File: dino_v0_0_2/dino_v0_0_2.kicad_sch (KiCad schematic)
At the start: 27 parts, among them Q1 Write Button Gate, U1 Quad AND

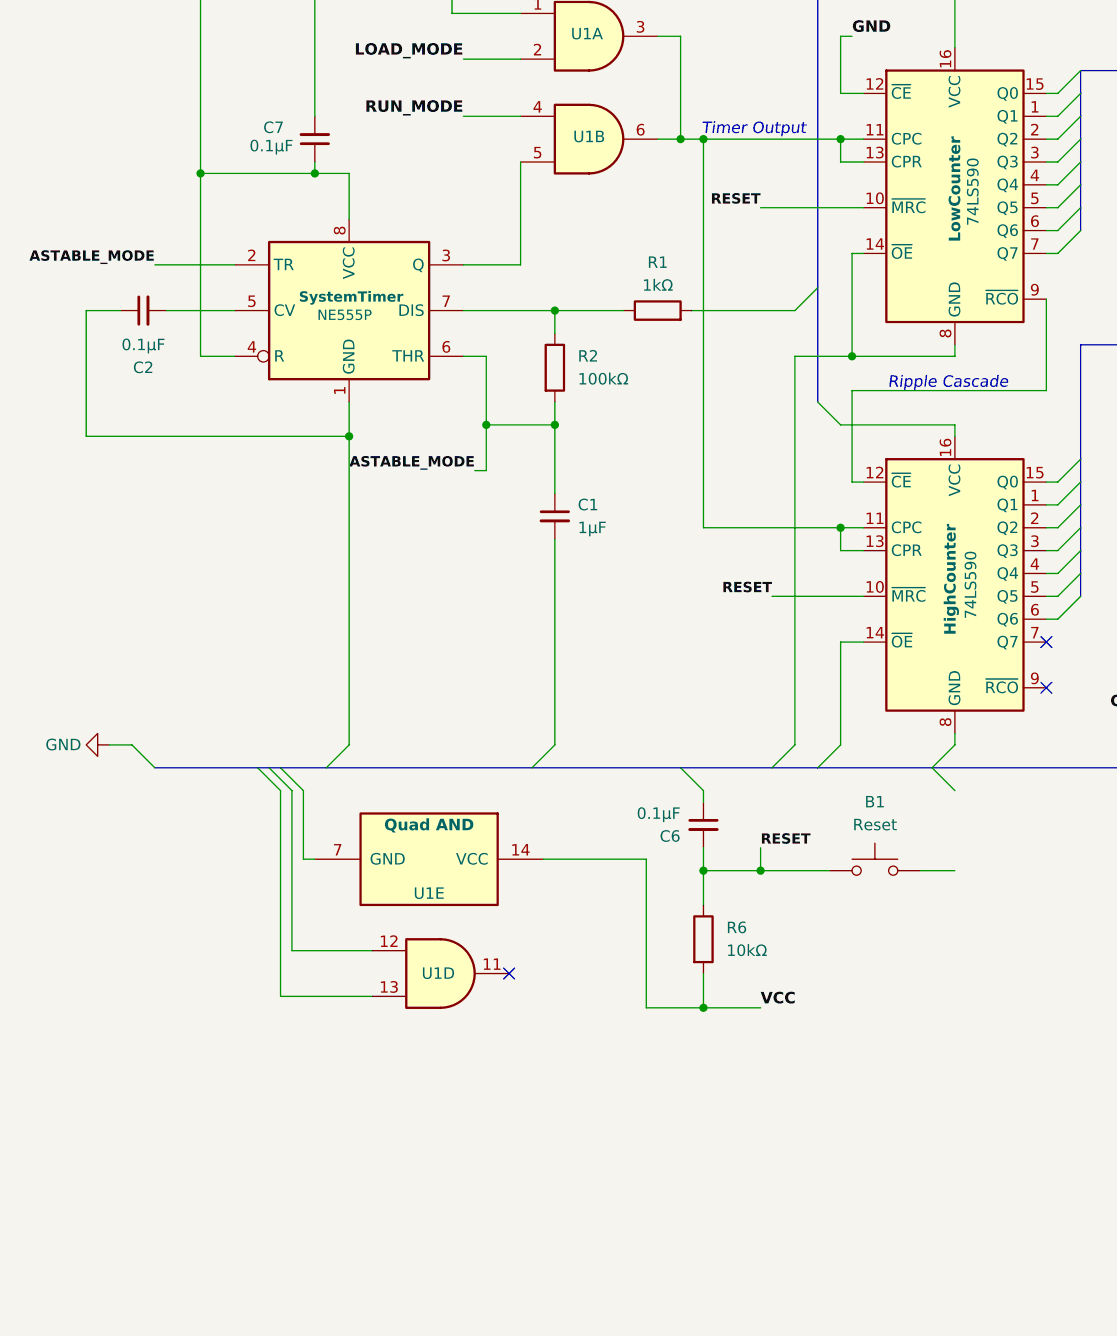
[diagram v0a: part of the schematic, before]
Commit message: Migrates project to version 0.0.2 with Ring Counter addition
Renames existing project files from version 0.0.1 to 0.0.2 to reflect updates.
Adds a new sub-circuit named "RingCounter" to the schematic, improving functionality.
Updates date and revision information in title blocks to keep documentation current.
Integrates new wires, junctions, and labels into existing schematics to accommodate the RingCounter.
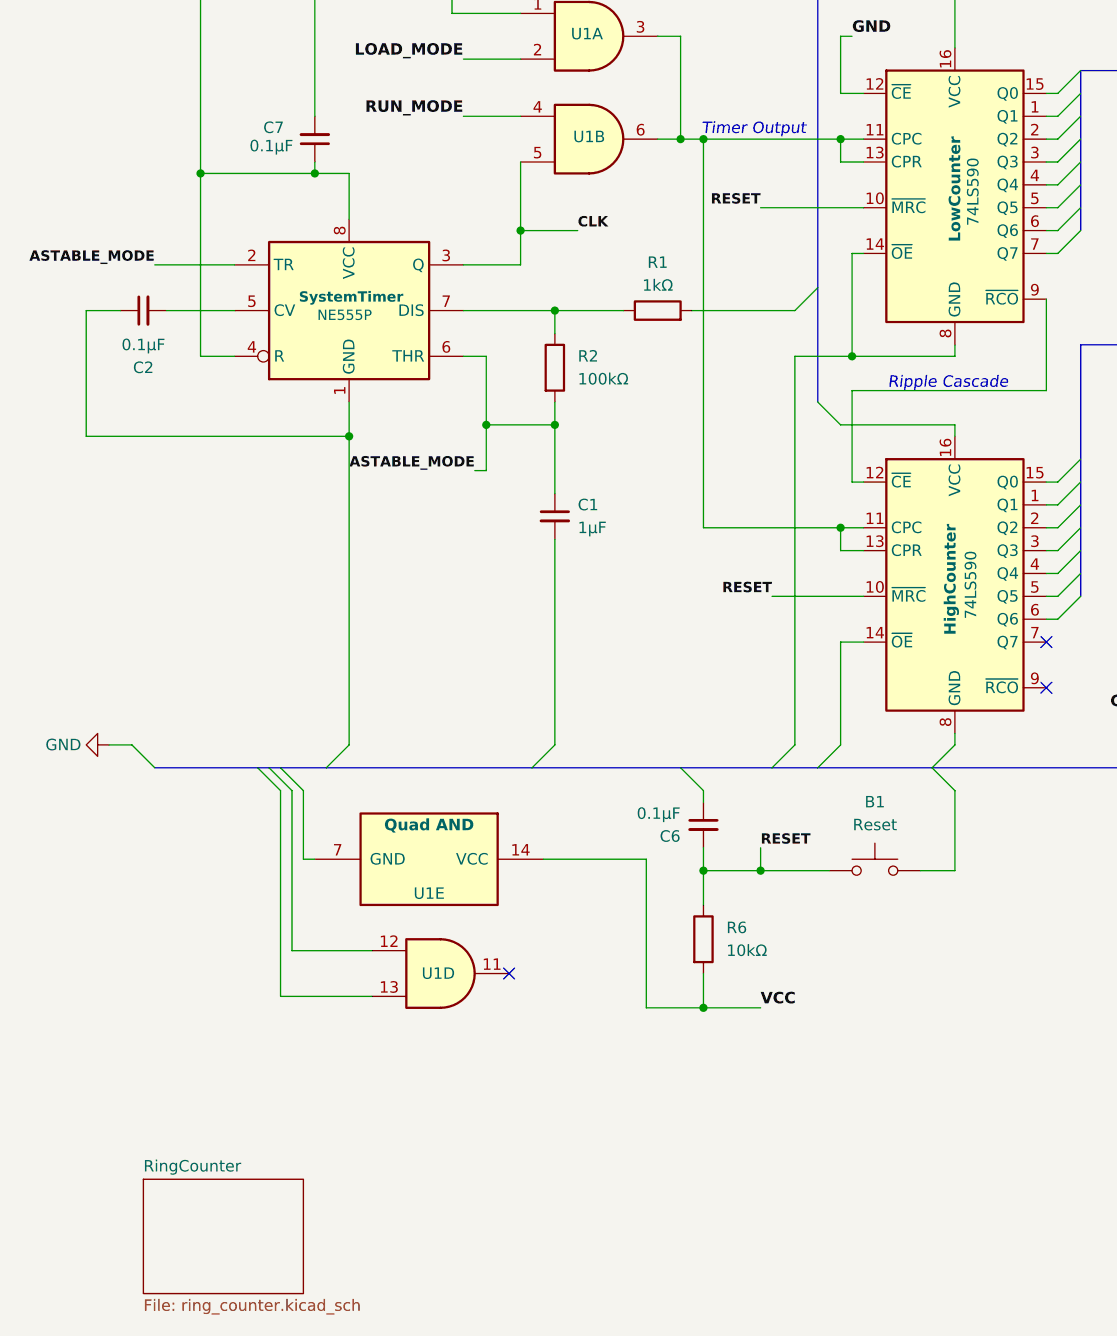
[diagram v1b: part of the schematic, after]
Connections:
- net CLK: now reaches SystemTimer.3 (Q), U1.5
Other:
- added sheet RingCounter (ring_counter.kicad_sch)
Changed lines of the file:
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@@
 	(title_block
 		(title "Dino v0.0.1")
-		(date "2025-07-02")
-		(rev "v1.0.3")
+		(date "2025-07-18")
+		(rev "v1.0.4")
 		(comment 1 "Core Components")
 		(comment 3 "Utilizes a 555 timer and binary counter to increment addressing.")
@@
 	)
 	(junction
+		(at 67.31 72.39)
+		(diameter 0)
+		(color 0 0 0 0)
+	)
+	(junction
 		(at 199.39 69.85)
 		(diameter 0)
@@
 	(wire
 		(pts
+			(xy 67.31 72.39) (xy 73.66 72.39)
+		)
+		(stroke
+			(width 0)
+			(type default)
+		)
+	)
+	(wire
+		(pts
 			(xy 97.79 86.36) (xy 104.14 86.36)
 		)
@@
 	(wire
 		(pts
-			(xy 67.31 76.2) (xy 67.31 64.77)
+			(xy 67.31 76.2) (xy 67.31 72.39)
 		)
 		(stroke
@@
 	(wire
 		(pts
+			(xy 67.31 72.39) (xy 67.31 64.77)
+		)
+		(stroke
+			(width 0)
+			(type default)
+		)
+	)
+	(wire
+		(pts
 			(xy 19.05 95.25) (xy 48.26 95.25)
 		)
@@
 	(wire
 		(pts
+			(xy 115.57 134.62) (xy 115.57 143.51)
+		)
+		(stroke
+			(width 0)
+			(type default)
+		)
+	)
+	(wire
+		(pts
 			(xy 125.73 100.33) (xy 127 100.33)
 		)
@@
 		)
 	)
+	(label "CLK"
+		(at 73.66 72.39 0)
+		(effects
+			(font
+				(size 1.143 1.143)
+				(thickness 0.254)
+				(bold yes)
+			)
+			(justify left bottom)
+		)
+	)
 	(label "LOAD_MODE"
 		(at 60.96 53.34 180)
@@
 				)
 			)
+		)
+	)
+	(sheet
+		(at 25.4 177.8)
+		(size 17.78 12.7)
+		(exclude_from_sim no)
+		(in_bom yes)
+		(on_board yes)
+		(dnp no)
+		(fields_autoplaced yes)
+		(stroke
+			(width 0.1524)
+			(type solid)
+		)
+		(fill
+			(color 0 0 0 0.0000)
+		)
+		(property "Sheetname" "RingCounter"
+			(at 25.4 177.0884 0)
+			(effects
+				(font
+					(size 1.27 1.27)
+				)
+				(justify left bottom)
+			)
+		)
+		(property "Sheetfile" "ring_counter.kicad_sch"
+			(at 25.4 191.0846 0)
+			(effects
+				(font
+					(size 1.27 1.27)
+				)
+				(justify left top)
+			)
+		)
+		(instances
+			(project "dino_v0_0_1"
+				(path "/e43166a5-d972-471d-b3cf-9f4f12c7f541"
+					(page "3")
+				)
+			)

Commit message: Dino v0.0.2 Schematic Update
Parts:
- removed B1: Reset, symbol Switch:SW_Push
- removed B2: Write, symbol Switch:SW_Push
- removed B3: Inc Addr, symbol Switch:SW_Push
- removed Bus-Arbiter: 74LS645, symbol 74xx:74LS645
- removed C3, C4, C5, C6: 0.1µF, symbol Device:C_Small
- removed HighCounter, LowCounter: 74LS590, symbol 74xx:74LS590
- removed MCM60256AP: SRAM, symbol Memory_RAM:MCM60256AP
- removed Q1: Write Button Gate, Package_TO_SOT_THT:TO-92_Inline, symbol Transistor_BJT:2N3904
- removed R3, R4, R5, R6, R7, R8: 10kΩ, symbol Device:R
- removed SPDT: LOAD/RUN, symbol Switch:SW_SPDT
- removed U1: Quad AND, symbol 74xx:74LS08
- added U5: 7400, symbol 74xx:7400
- added U6: 74LS163, symbol 74xx:74LS163
- added U7: 74LS138, symbol 74xx:74LS138
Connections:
- net GND: now also C1.2, C2.1, C7.1, SystemTimer.1 (GND), U5.7 (GND), U6.3 (D0), U6.4 (D1), U6.5 (D2), U6.6 (D3), U6.8 (GND), U7.4 (E1), U7.5 (E2), U7.8 (GND); no longer C7.2
- net +5V: now reaches SystemTimer.4 (R), SystemTimer.8 (VCC)
- net +5V: now also C7.2, C8.2, R1.2, U5.14 (VCC), U6.10 (CET), U6.16 (VCC), U6.7 (CEP), U6.9 (~{PE}), U7.16 (VCC), U7.6 (E3); no longer C7.1
- net ASTABLE_MODE: no longer names the net of C1.1, R2.2, SystemTimer.2 (TR), SystemTimer.6 (THR)
- net CLK: no longer names the net of SystemTimer.3 (Q)
- net CLK: now also U6.2 (CP)
- new net: U6.14 (Q0), U7.1 (A0)
- new net: U5.1, U6.13 (Q1), U7.2 (A1)
- new net: U5.2, U6.12 (Q2), U7.3 (A2)
- new net: U5.3, U6.1 (~{MR})
- no-connect marks 3 -> 19
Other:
- sheet RingCounter renamed Data
- sheet Data: file ring_counter.kicad_sch -> data.kicad_sch
- note removed: "+5V"
- note removed: "Output Enable"
- note removed: "Ripple Cascade"
- note removed: "Timer Output"
- note removed: "Write Pulse"
- title: Dino v0.0.1 -> Dino v0.0.2
- moved on the sheet: C1, C2, C7, R1, R2, SystemTimer

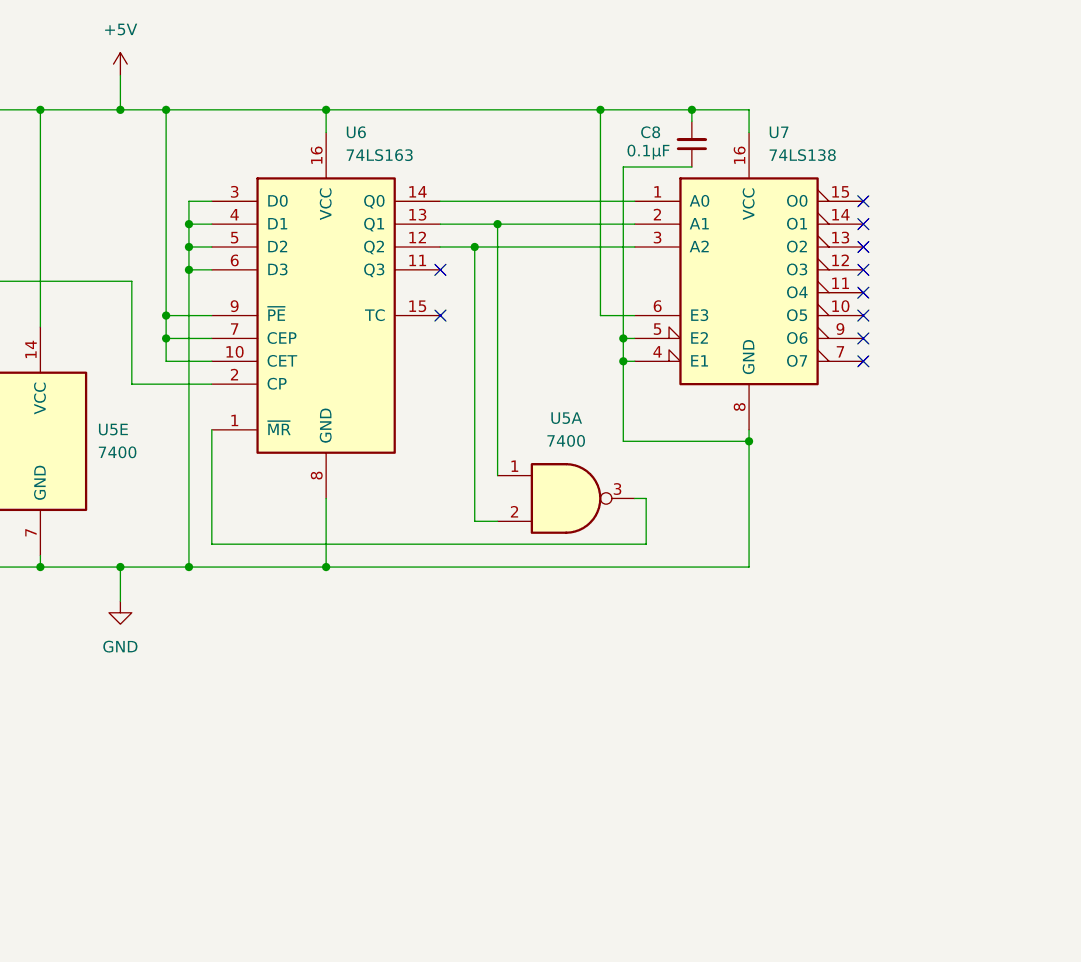
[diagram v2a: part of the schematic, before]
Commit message: Updates schematics for improved circuit design
Revises date and revision comments across schematics for consistency
Modifies component descriptions to reflect accurate functionality
Adds new junctions and wires for improved connectivity in the circuit
Inserts new capacitors and logic decoders to enhance circuit performance

Includes changes to the title block and project metadata for clarity
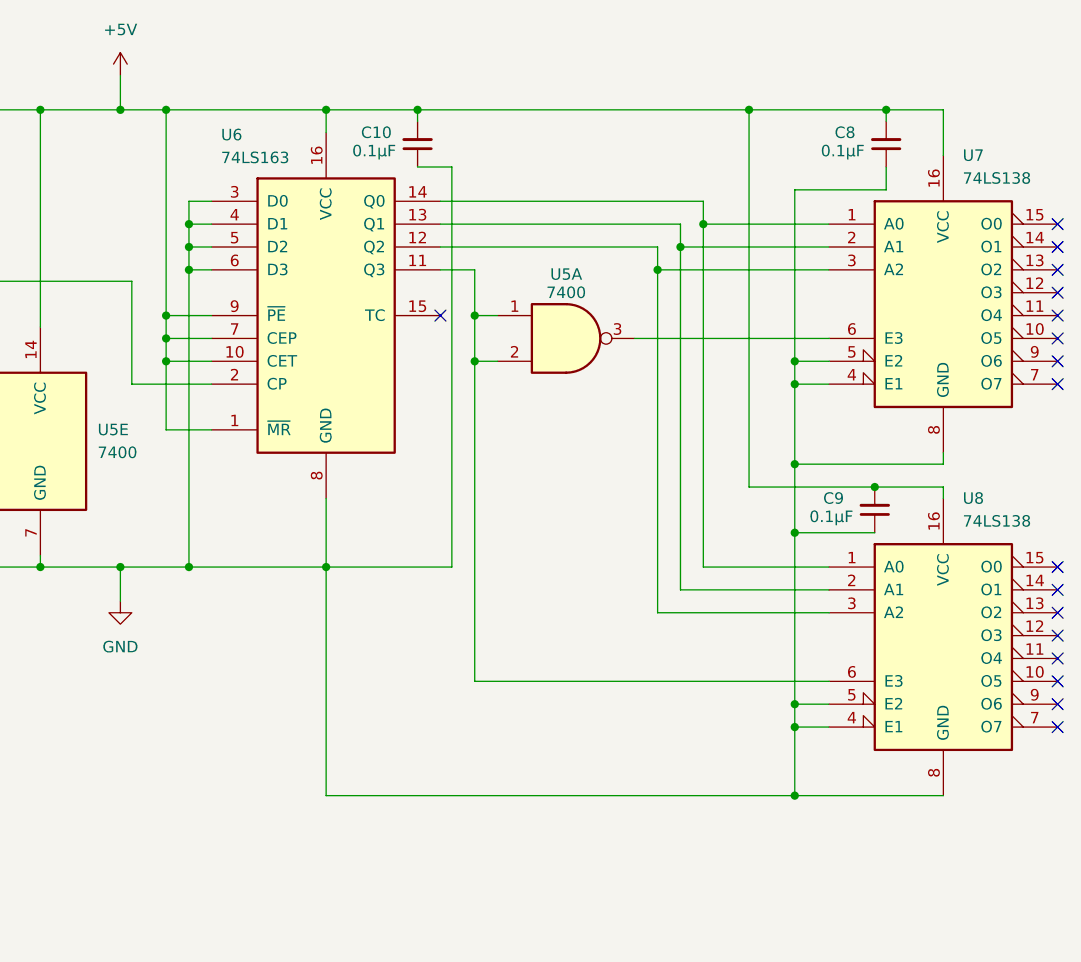
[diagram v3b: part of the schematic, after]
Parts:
- added C10, C9: 0.1µF, symbol Device:C_Small
- added U8: 74LS138, symbol 74xx:74LS138
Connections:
- net +5V: now also U6.1 (~{MR}), C10.2, C9.2, U8.16 (VCC); no longer U7.6 (E3)
- net GND: now also C10.1, C9.1, U8.4 (E1), U8.5 (E2), U8.8 (GND)
- net at U6.14 (Q0), U7.1 (A0): now also U8.1 (A0)
- net at U6.13 (Q1), U7.2 (A1): now also U8.2 (A1); no longer U5.1
- net at U6.12 (Q2), U7.3 (A2): now also U8.3 (A2); no longer U5.2
- net at U5.3: now also U7.6 (E3); no longer U6.1 (~{MR})
- net at U6.11 (Q3): now also U5.1, U5.2, U8.6 (E3)
- no-connect marks 19 -> 26
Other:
- moved on the sheet: C8, U5A, U7

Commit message: DINO Updates
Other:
- sheet Data renamed T0_T1_Decoder
- sheet Input-Output Sheet renamed 4
- added sheet Program Counter (program_counter.kicad_sch)
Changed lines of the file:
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@@
 	(title_block
 		(title "Dino v0.0.2")
-		(date "2025-07-24")
-		(rev "v1.0.5")
+		(date "2025-07-28")
+		(rev "v1.0.7")
 		(comment 1 "Control Unit - 16 1-hot inverted timing stages")
 		(comment 3 "An 8-bit computer with 16-bit addressing and 16-bit control words")
@@
 	)
 	(sheet
-		(at 25.4 177.8)
+		(at 88.9 119.38)
 		(size 17.78 12.7)
 		(exclude_from_sim no)
@@
 			(color 0 0 0 0.0000)
 		)
-		(property "Sheetname" "Data"
-			(at 25.4 177.0884 0)
+		(property "Sheetname" "T0_T1_Decoder"
+			(at 88.9 118.6684 0)
 			(effects
 				(font
@@
 		)
 		(property "Sheetfile" "data.kicad_sch"
-			(at 25.4 191.0846 0)
+			(at 88.9 132.6646 0)
+			(effects
+				(font
+					(size 1.27 1.27)
+				)
+				(justify left top)
+			)
+		)
+		(instances
+			(project "dino_v0_0_2"
+				(path "/e43166a5-d972-471d-b3cf-9f4f12c7f541"
+					(page "3")
+				)
+			)
+		)
+	)
+	(sheet
+		(at 54.61 147.32)
+		(size 15.24 12.7)
+		(exclude_from_sim no)
+		(in_bom yes)
+		(on_board yes)
+		(dnp no)
+		(stroke
+			(width 0.1524)
+			(type solid)
+		)
+		(fill
+			(color 0 0 0 0.0000)
+		)
+		(property "Sheetname" "4"
+			(at 53.594 167.132 0)
+			(effects
+				(font
+					(size 1.27 1.27)
+				)
+				(justify left bottom)
+			)
+		)
+		(property "Sheetfile" "input_output.kicad_sch"
+			(at 50.546 167.894 0)
+			(effects
+				(font
+					(size 1.27 1.27)
+				)
+				(justify left top)
+				(hide yes)
+			)
+		)
+		(instances
+			(project "dino_v0_0_2"
+				(path "/e43166a5-d972-471d-b3cf-9f4f12c7f541"
+					(page "3")
+				)
+			)
+		)
+	)
+	(sheet
+		(at 54.61 119.38)
+		(size 16.51 12.7)
+		(exclude_from_sim no)
+		(in_bom yes)
+		(on_board yes)
+		(dnp no)
+		(fields_autoplaced yes)
+		(stroke
+			(width 0.1524)
+			(type solid)
+		)
+		(fill
+			(color 0 0 0 0.0000)
+		)
+		(property "Sheetname" "Program Counter"
+			(at 54.61 118.6684 0)
+			(effects
+				(font
+					(size 1.27 1.27)
+				)
+				(justify left bottom)
+			)
+		)
+		(property "Sheetfile" "program_counter.kicad_sch"
+			(at 54.61 132.6646 0)
 			(effects
 				(font
@@
 				)
 			)
-		)
-	)
-	(sheet
-		(at 52.07 175.26)
-		(size 17.145 17.78)
-		(exclude_from_sim no)
-		(in_bom yes)
-		(on_board yes)
-		(dnp no)
-		(stroke
-			(width 0.1524)
-			(type solid)
-		)
-		(fill
-			(color 0 0 0 0.0000)
-		)
-		(property "Sheetname" "Input-Output Sheet"
-			(at 51.054 195.072 0)
-			(effects
-				(font
-					(size 1.27 1.27)
-				)
-				(justify left bottom)
-			)
-		)
-		(property "Sheetfile" "input_output.kicad_sch"
-			(at 48.006 195.834 0)
-			(effects
-				(font
-					(size 1.27 1.27)
-				)
-				(justify left top)
-				(hide yes)
-			)
-		)
-		(instances
-			(project "dino_v0_0_2"
-				(path "/e43166a5-d972-471d-b3cf-9f4f12c7f541"
-					(page "3")
-				)
-			)

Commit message: Update
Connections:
- no-connect marks 26 -> 10
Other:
- sheet 4 renamed Output
- sheet T0_T1_Decoder renamed Microcode_Decoder
- added sheet Control Word Module (control_word.kicad_sch)
- added sheet Memory (memory.kicad_sch)
- added sheet Memory Data Register (mdr.kicad_sch)
- added sheet Register Modules (registers.kicad_sch)
- sheet Microcode_Decoder: file data.kicad_sch -> microcode.kicad_sch
- moved on the sheet: C1, C10, C2, C7, C8, C9, R1, R2, SystemTimer, U5A, U5B, U5C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

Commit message: Schematics WIP
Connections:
- net CLK: now reaches SystemTimer.3 (Q), U6.2 (CP)
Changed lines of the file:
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@@
+	)
+	(junction
+		(at 92.71 105.41)
+		(diameter 0)
+		(color 0 0 0 0)
 	)
 	(junction
@@
 		)
 	)
-	(wire
-		(pts
-			(xy 95.25 105.41) (xy 95.25 116.84)
-		)
-		(stroke
-			(width 0)
-			(type default)
-		)
-	)
 	(bus
 		(pts
@@
 	(wire
 		(pts
+			(xy 92.71 102.87) (xy 92.71 105.41)
+		)
+		(stroke
+			(width 0)
+			(type default)
+		)
+	)
+	(wire
+		(pts
 			(xy 199.39 121.92) (xy 213.36 121.92)
 		)
@@
 	(wire
 		(pts
-			(xy 57.15 105.41) (xy 95.25 105.41)
+			(xy 57.15 105.41) (xy 92.71 105.41)
 		)
 		(stroke
@@
 	(wire
 		(pts
+			(xy 92.71 105.41) (xy 92.71 116.84)
+		)
+		(stroke
+			(width 0)
+			(type default)
+		)
+	)
+	(wire
+		(pts
 			(xy 168.91 116.84) (xy 172.72 116.84)
 		)
@@
 	(wire
 		(pts
-			(xy 95.25 116.84) (xy 104.14 116.84)
+			(xy 92.71 116.84) (xy 104.14 116.84)
 		)
 		(stroke
@@
 		(effects
 			(font
+				(size 1.27 1.27)
+			)
+			(justify left bottom)
+		)
+	)
+	(label "CLK"
+		(at 92.71 102.87 0)
+		(effects
+			(font

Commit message: KiCAD Updates
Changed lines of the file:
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@@
 		)
 	)
-	(label "Control Word"
+	(label "One-Hot Inverted State"
 		(at 215.9 91.44 0)
 		(effects
